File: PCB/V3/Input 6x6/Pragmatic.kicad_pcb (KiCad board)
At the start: 2 copper layers, 114.3 x 127 mm, 82 parts, among them J1 Hand-Soldering, SW1 SW_Push, SW10 SW_Push, SW11 SW_Push, SW12 SW_Push, SW13 SW_Push, SW14 SW_Push, SW15 SW_Push, SW16 SW_Push, SW17 SW_Push, SW18 SW_Push, SW19 SW_Push, SW2 SW_Push, SW20 SW_Push, SW21 SW_Push, SW22 SW_Push, SW23 SW_Push, SW24 SW_Push, SW25 SW_Push, SW26 SW_Push, SW27 SW_Push, SW28 SW_Push, SW29 SW_Push, SW3 SW_Push, SW30 SW_Push, SW31 SW_Push, SW32 SW_Push, SW33 SW_Push, SW34 SW_Push, SW35 SW_Push, SW36 SW_Push, SW4 SW_Push, SW5 SW_Push, SW6 SW_Push, SW7 SW_Push, SW8 SW_Push, SW9 SW_Push

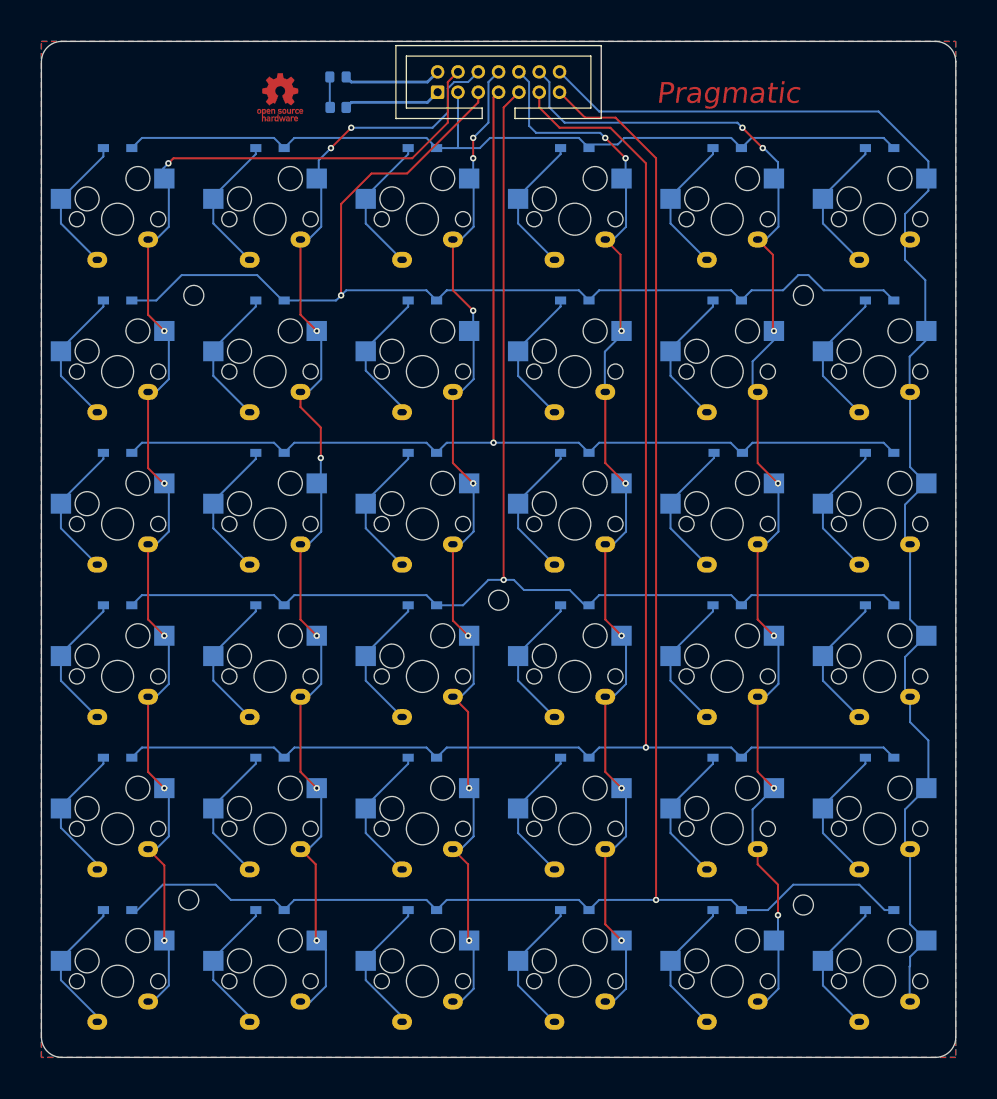
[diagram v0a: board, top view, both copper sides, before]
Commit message: increase plate border for manufacture.
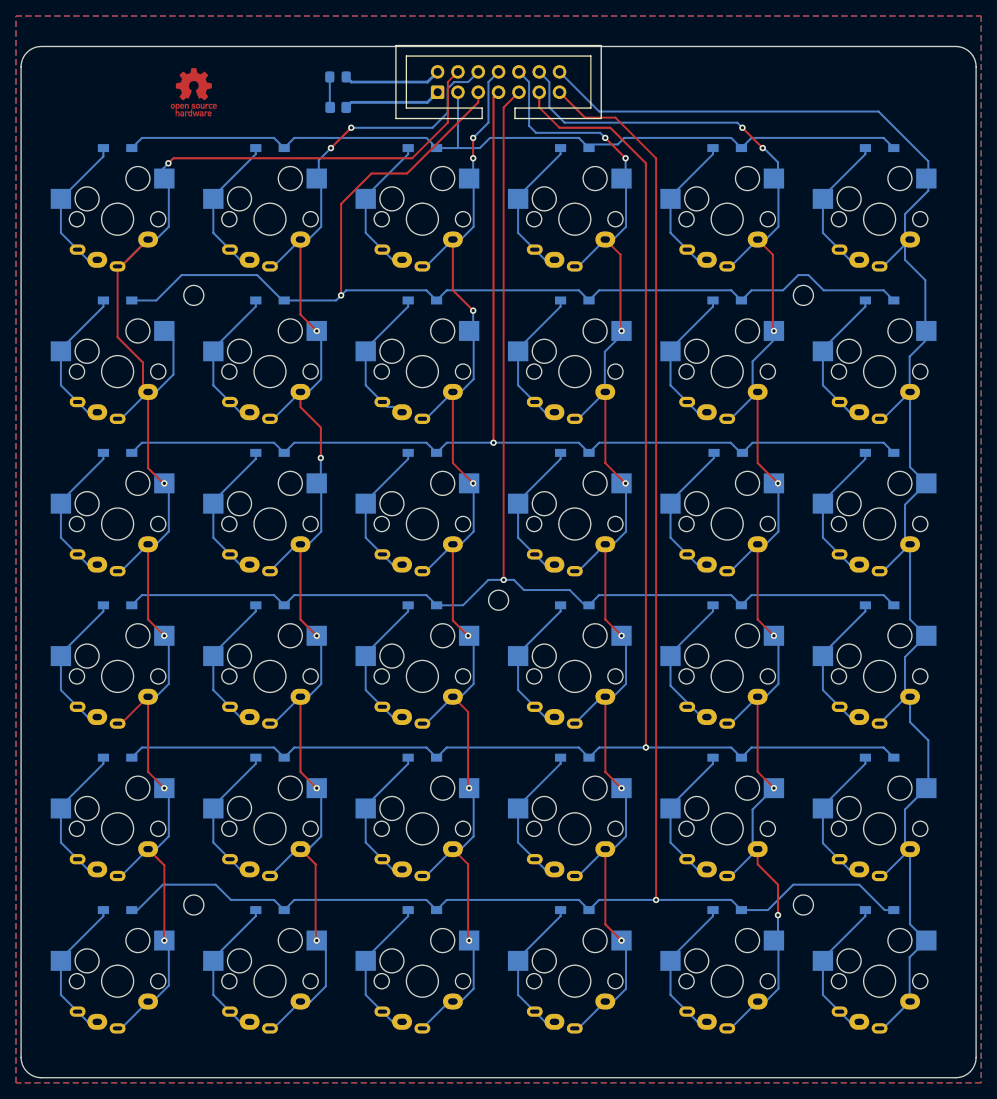
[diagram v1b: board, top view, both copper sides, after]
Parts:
- SW1, SW10, SW11, SW12, SW13, SW14, SW15, SW16, SW17, SW18, SW19, SW2, SW20, SW21, SW22, SW23, SW24, SW25, SW26, SW27, SW28, SW29, SW3, SW30, SW31, SW32, SW33, SW34, SW35, SW36, SW4, SW5, SW6, SW7, SW8, SW9: footprint Keyboard_JSA:MX_Hotswap_MX_Solder -> Keyboard_JSA:MX_Hotswap_MX_Choc_Solder
- moved LOGO1 10.8 mm to (66.7, 41.3)
- moved H2 0.90 mm to (66.7, 142.9)
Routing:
- net Col1: track 153.5 -> 195.1 mm, vias 6 -> 5
- net Col5: track 145.8 -> 177.0 mm
- net Col2: track 137.8 -> 169.0 mm
- net Col4: track 131.4 -> 162.6 mm
- net Col3: track 122.2 -> 153.4 mm
- net Col6: track 163.8 -> 195.0 mm
- net Net-(D31-Pad2): track 17.5 -> 19.1 mm
- net Net-(D33-Pad2): track 17.5 -> 18.9 mm
- net Net-(D32-Pad2): track 17.5 -> 18.9 mm
- net Net-(D25-Pad2): track 17.5 -> 18.9 mm
- net Net-(D9-Pad2): track 17.5 -> 18.6 mm
- net Net-(D30-Pad2): track 18.2 -> 18.9 mm
- net Net-(D35-Pad2): track 18.2 -> 18.9 mm
- net Net-(D34-Pad2): track 18.2 -> 18.9 mm
- net Net-(D16-Pad2): track 18.2 -> 18.9 mm
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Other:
- board size 114.3 x 127 mm -> 119.4 x 128.9 mm
- board text added: "V3.1"
- board text removed: "V3 Hotswap"
